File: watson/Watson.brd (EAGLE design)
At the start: 104.1 x 58.4 mm, 38 parts, among them X1 2540-FLAT

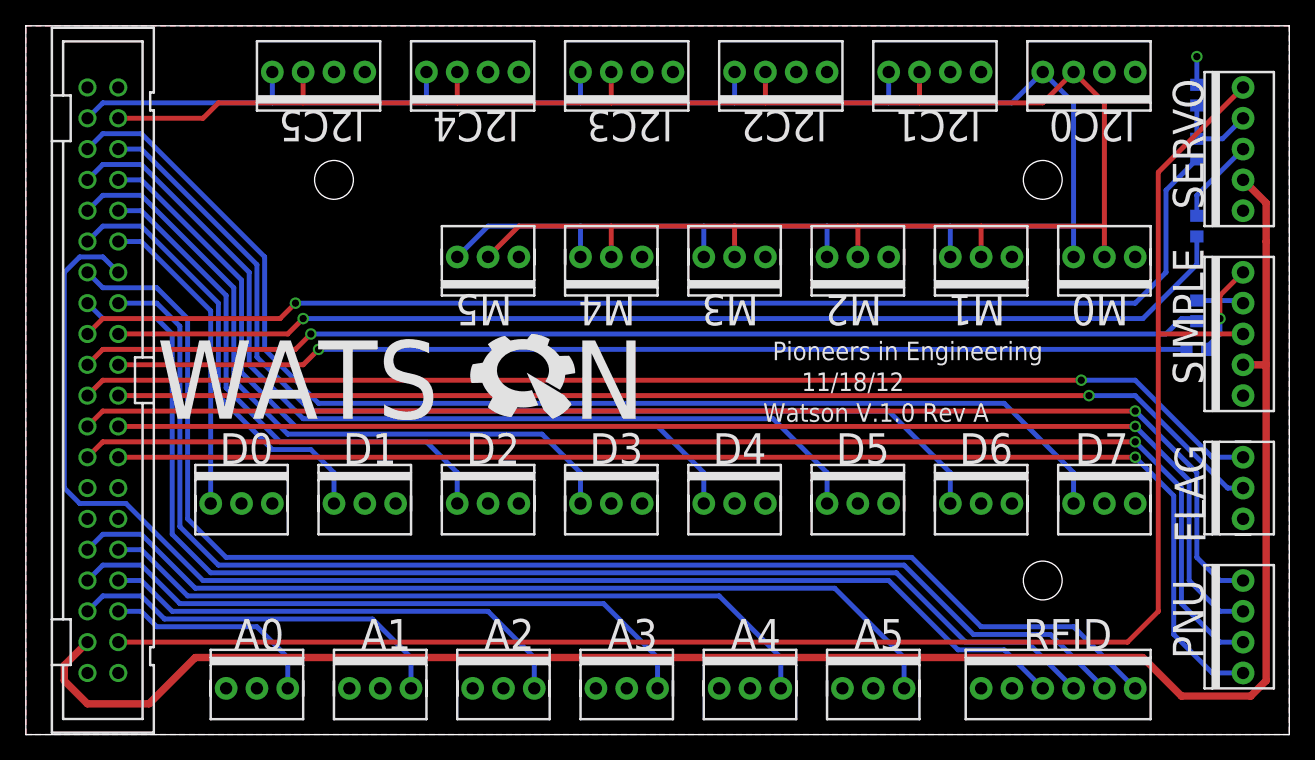
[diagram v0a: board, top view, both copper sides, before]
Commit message: Fix all boards to be at origin, fix dimension width to be 10 mil
Change-Id: I08bc507f450d0f63cfcc98eecb1f52bd6fb958a5
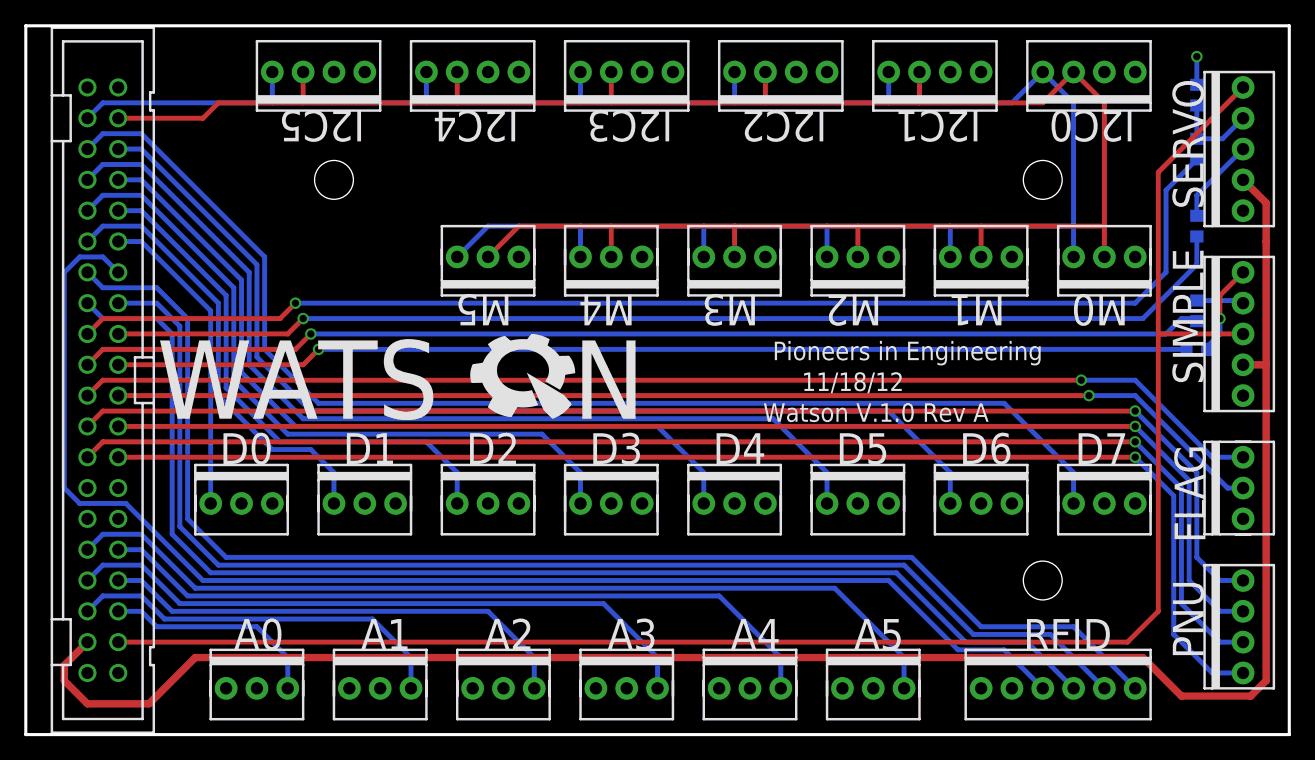
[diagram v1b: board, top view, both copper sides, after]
